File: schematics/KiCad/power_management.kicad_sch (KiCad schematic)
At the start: 19 parts, among them J3 USB_C, Q1 DMG6601LVT-7, U2 AP2112K-3.3, U4 CH340C, U5 MP2615AGQ-Z

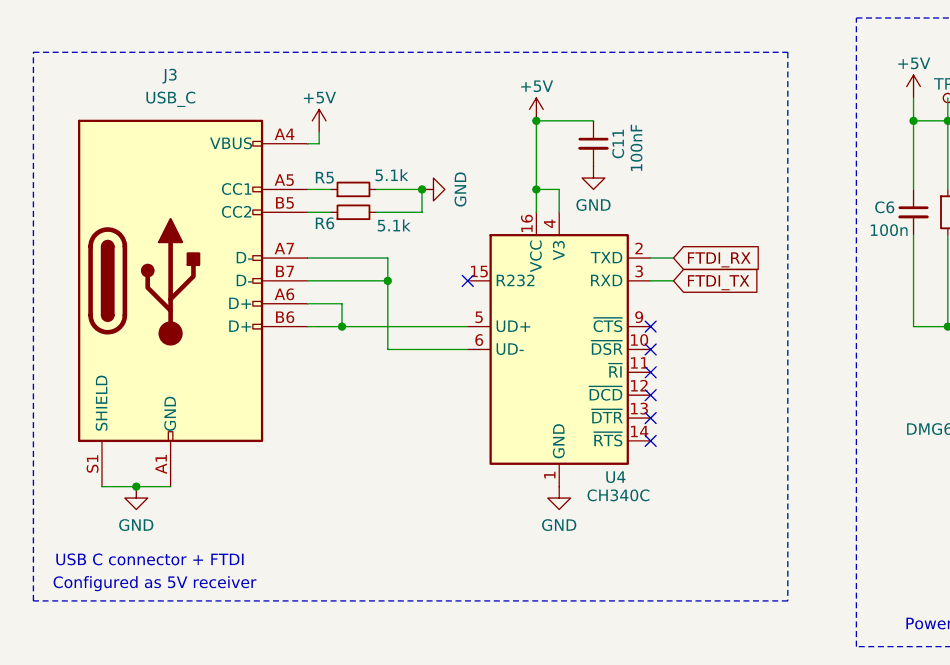
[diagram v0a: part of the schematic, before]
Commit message: move FTDI chip back to main page
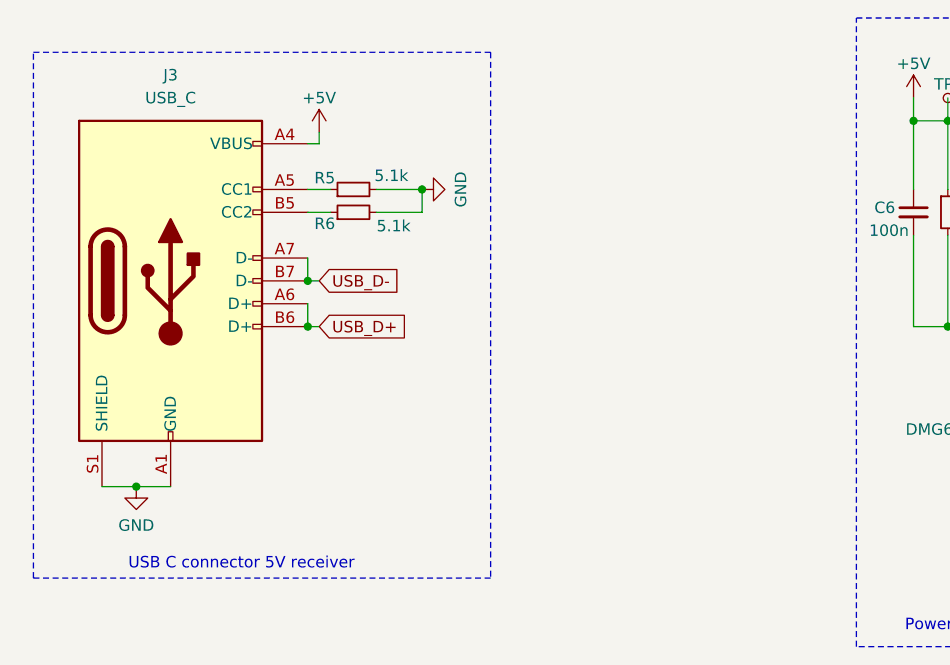
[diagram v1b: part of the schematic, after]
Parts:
- removed C11: 100nF, Capacitor_SMD:C_0201_0603Metric, symbol Device:C_Small
- removed U4: CH340C, Package_SO:SOIC-16_3.9x9.9mm_P1.27mm, symbol Interface_USB:CH340C
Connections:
- net USB_D+: now reaches J3.A6 (D+), J3.B6 (D+)
- net USB_D-: now reaches J3.A7 (D-), J3.B7 (D-)
- no-connect marks 7 -> 0
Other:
- note added: "USB C connector 5V receiver"
- note removed: "Configured as 5V receiver"
- note removed: "USB C connector + FTDI"

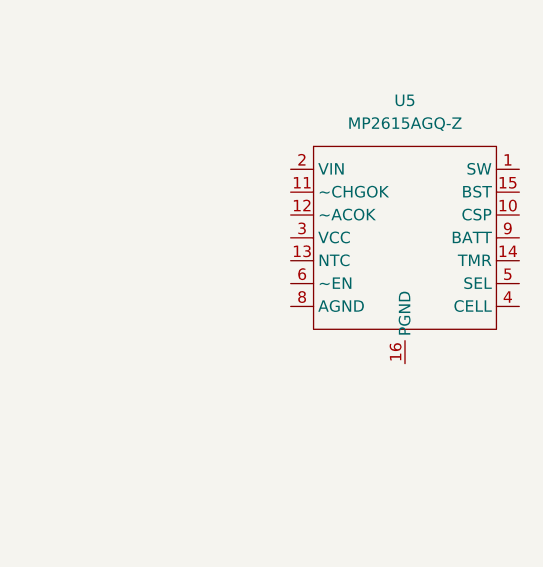
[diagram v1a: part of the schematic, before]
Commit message: reorganise symbols
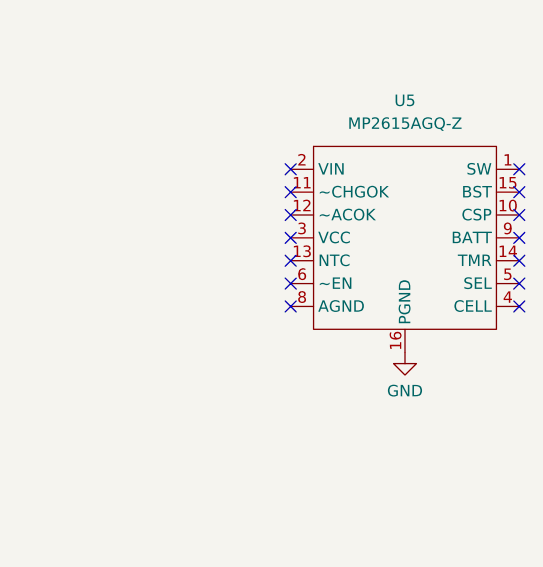
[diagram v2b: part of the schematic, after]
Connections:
- net GND: now also U5.16 (PGND)
- net at U5.7 (NC): no longer U5.16 (PGND)
- no-connect marks 0 -> 14
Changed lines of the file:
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@@
 		(color 0 0 0 0)
+	)
+	(no_connect
+		(at 252.73 91.44)
+	)
+	(no_connect
+		(at 227.33 99.06)
+	)
+	(no_connect
+		(at 227.33 91.44)
+	)
+	(no_connect
+		(at 227.33 88.9)
+	)
+	(no_connect
+		(at 252.73 86.36)
+	)
+	(no_connect
+		(at 227.33 96.52)
+	)
+	(no_connect
+		(at 252.73 96.52)
+	)
+	(no_connect
+		(at 252.73 88.9)
+	)
+	(no_connect
+		(at 252.73 93.98)
+	)
+	(no_connect
+		(at 227.33 86.36)
+	)
+	(no_connect
+		(at 252.73 99.06)
+	)
+	(no_connect
+		(at 227.33 93.98)
+	)
+	(no_connect
+		(at 227.33 101.6)
+	)
+	(no_connect
+		(at 252.73 101.6)
 	)
 	(wire
@@
 	)
 	(symbol
-		(lib_id "leany-symbols:DMG6601LVT-7")
-		(at 139.7 72.39 270)
-		(mirror x)
-		(unit 2)
-		(exclude_from_sim no)
-		(in_bom yes)
-		(on_board yes)
-		(dnp no)
-		(property "Reference" "Q1"
-			(at 139.7 66.04 90)
-			(effects
-				(font
-					(size 1.27 1.27)
-				)
-			)
-		)
-		(property "Value" "DMG6601LVT-7"
-			(at 139.7 68.58 90)
-			(effects
-				(font
-					(size 1.27 1.27)
-				)
-			)
-		)
-		(property "Footprint" "Package_TO_SOT_SMD:TSOT-23-6"
-			(at 137.795 69.85 0)
-			(effects
-				(font
-					(size 1.27 1.27)
-				)
-				(justify left)
-				(hide yes)
-			)
-		)
-		(property "Datasheet" "https://www.diodes.com/assets/Datasheets/DMG6601LVT.pdf"
-			(at 135.89 69.85 0)
-			(effects
-				(font
-					(size 1.27 1.27)
-				)
-				(justify left)
-				(hide yes)
-			)
-		)
-		(property "Description" "3.6A/-2.1A Id, 30V Vds, Complementary pair enhancement mode P-Channel and N-Channel MOSFET, TSOT-23-6"
-			(at 139.7 72.39 0)
-			(effects
-				(font
-					(size 1.27 1.27)
-				)
-				(hide yes)
-			)
-		)
-		(pin "1"
-		)
-		(pin "2"
-		)
-		(pin "3"
-		)
-		(pin "4"
-		)
-		(pin "5"
-		)
-		(pin "6"
-		)
-		(instances
-			(project "leany"
-				(path "/e47b2519-93ca-4a48-9414-ecc253dd35f5/702fc064-eab2-4b82-8f62-a654ccd28f72"
-					(reference "Q1")
-					(unit 2)
-				)
-			)
-		)
-	)
-	(symbol
-		(lib_id "Device:R_Small")
-		(at 149.86 113.03 180)
-		(unit 1)
-		(exclude_from_sim no)
-		(in_bom yes)
-		(on_board yes)
-		(dnp no)
-		(property "Reference" "R4"
-			(at 145.796 111.76 90)
-			(effects
-				(font
-					(size 1.27 1.27)
-				)
-				(justify left)
-			)
-		)
-		(property "Value" "1M"
-			(at 147.828 111.506 90)
-			(effects
-				(font
-					(size 1.27 1.27)
-				)
-				(justify left)
-			)
-		)
-		(property "Footprint" "Resistor_SMD:R_0603_1608Metric"
-			(at 149.86 113.03 0)
-			(effects
-				(font
-					(size 1.27 1.27)
-				)
-				(hide yes)
-			)
-		)
-		(property "Datasheet" "~"
-			(at 149.86 113.03 0)
-			(effects
-				(font
-					(size 1.27 1.27)
-				)
-				(hide yes)
-			)
-		)
-		(property "Description" "Resistor, small symbol"
-			(at 149.86 113.03 0)
-			(effects
-				(font
-					(size 1.27 1.27)
-				)
-				(hide yes)
-			)
-		)
-		(pin "1"
-		)
-		(pin "2"
-		)
-		(instances
-			(project "leany"
-				(path "/e47b2519-93ca-4a48-9414-ecc253dd35f5/702fc064-eab2-4b82-8f62-a654ccd28f72"
-					(reference "R4")
-					(unit 1)
-				)
-			)
-		)
-	)
-	(symbol
 		(lib_id "leany-symbols:MP2615AGQ-Z")
 		(at 240.03 93.98 0)
@@
 			)
 		)
+		(pin "14"
+		)
 		(pin "4"
 		)
+		(pin "5"
+		)
+		(pin "11"
+		)
+		(pin "8"
+		)
+		(pin "13"
+		)
+		(pin "9"
+		)
 		(pin "7"
 		)
-		(pin "9"
+		(pin "10"
+		)
+		(pin "12"
+		)
+		(pin "1"
+		)
+		(pin "2"
+		)
+		(pin "6"
+		)
+		(pin "3"
 		)
 		(pin "15"
 		)
-		(pin "10"
+		(pin "16"
+		)
+		(instances
+			(project ""
+				(path "/e47b2519-93ca-4a48-9414-ecc253dd35f5/702fc064-eab2-4b82-8f62-a654ccd28f72"
+					(reference "U5")
+					(unit 1)
+				)
+			)
+		)
+	)
+	(symbol
+		(lib_id "leany-symbols:DMG6601LVT-7")
+		(at 139.7 72.39 270)
+		(mirror x)
+		(unit 2)
+		(exclude_from_sim no)
+		(in_bom yes)
+		(on_board yes)
+		(dnp no)
+		(property "Reference" "Q1"
+			(at 139.7 66.04 90)
+			(effects
+				(font
+					(size 1.27 1.27)
+				)
+			)
+		)
+		(property "Value" "DMG6601LVT-7"
+			(at 139.7 68.58 90)
+			(effects
+				(font
+					(size 1.27 1.27)
+				)
+			)
+		)
+		(property "Footprint" "Package_TO_SOT_SMD:TSOT-23-6"
+			(at 137.795 69.85 0)
+			(effects
+				(font
+					(size 1.27 1.27)
+				)
+				(justify left)
+				(hide yes)
+			)
+		)
+		(property "Datasheet" "https://www.diodes.com/assets/Datasheets/DMG6601LVT.pdf"
+			(at 135.89 69.85 0)
+			(effects
+				(font
+					(size 1.27 1.27)
+				)
+				(justify left)
+				(hide yes)
+			)
+		)
+		(property "Description" "3.6A/-2.1A Id, 30V Vds, Complementary pair enhancement mode P-Channel and N-Channel MOSFET, TSOT-23-6"
+			(at 139.7 72.39 0)
+			(effects
+				(font
+					(size 1.27 1.27)
+				)
+				(hide yes)
+			)
+		)
+		(pin "1"
 		)
 		(pin "2"
 		)
-		(pin "1"
-		)
-		(pin "12"
-		)
-		(pin "14"
-		)
-		(pin "8"
-		)
-		(pin "13"
-		)
-		(pin "16"
+		(pin "3"
+		)
+		(pin "4"
+		)
+		(pin "5"
 		)
 		(pin "6"
-		)
-		(pin "11"
-		)
-		(pin "3"
-		)
-		(pin "5"
 		)
 		(instances
 			(project "leany"
 				(path "/e47b2519-93ca-4a48-9414-ecc253dd35f5/702fc064-eab2-4b82-8f62-a654ccd28f72"
-					(reference "U5")
+					(reference "Q1")
+					(unit 2)
+				)
+			)
+		)
+	)
+	(symbol
+		(lib_id "Device:R_Small")
+		(at 149.86 113.03 180)
+		(unit 1)
+		(exclude_from_sim no)
+		(in_bom yes)
+		(on_board yes)
+		(dnp no)
+		(property "Reference" "R4"
+			(at 145.796 111.76 90)
+			(effects
+				(font
+					(size 1.27 1.27)
+				)
+				(justify left)
+			)
+		)
+		(property "Value" "1M"
+			(at 147.828 111.506 90)
+			(effects
+				(font
+					(size 1.27 1.27)
+				)
+				(justify left)
+			)
+		)
+		(property "Footprint" "Resistor_SMD:R_0603_1608Metric"
+			(at 149.86 113.03 0)
+			(effects
+				(font
+					(size 1.27 1.27)
+				)
+				(hide yes)
+			)
+		)
+		(property "Datasheet" "~"
+			(at 149.86 113.03 0)
+			(effects
+				(font
+					(size 1.27 1.27)
+				)
+				(hide yes)
+			)
+		)
+		(property "Description" "Resistor, small symbol"
+			(at 149.86 113.03 0)
+			(effects
+				(font
+					(size 1.27 1.27)
+				)
+				(hide yes)
+			)
+		)
+		(pin "1"
+		)
+		(pin "2"
+		)
+		(instances
+			(project "leany"
+				(path "/e47b2519-93ca-4a48-9414-ecc253dd35f5/702fc064-eab2-4b82-8f62-a654ccd28f72"
+					(reference "R4")
 					(unit 1)
 				)
@@
 					(unit 1)
 				)
+			)
+		)
+	)
+	(symbol
+		(lib_id "power:GND")
+		(at 240.03 106.68 0)
+		(unit 1)
+		(exclude_from_sim no)
+		(in_bom yes)
+		(on_board yes)
+		(dnp no)
+		(property "Reference" "#PWR028"
+			(at 240.03 113.03 0)
+			(effects
+				(font
+					(size 1.27 1.27)
+				)
+				(hide yes)
+			)
+		)
+		(property "Value" "GND"
+			(at 240.03 110.998 0)
+			(effects
+				(font
+					(size 1.27 1.27)
+				)
+			)
+		)
+		(property "Footprint" ""
+			(at 240.03 106.68 0)
+			(effects
+				(font
+					(size 1.27 1.27)
+				)
+				(hide yes)
+			)
+		)
+		(property "Datasheet" ""
+			(at 240.03 106.68 0)
+			(effects
+				(font
+					(size 1.27 1.27)
+				)
+				(hide yes)
+			)
+		)
+		(property "Description" "Power symbol creates a global label with name \"GND\" , ground"
+			(at 240.03 106.68 0)
+			(effects
+				(font
+					(size 1.27 1.27)
+				)
+				(hide yes)
+			)
+		)
+		(pin "1"
+		)
+		(instances
+			(project "leany"
+				(path "/e47b2519-93ca-4a48-9414-ecc253dd35f5/702fc064-eab2-4b82-8f62-a654ccd28f72"
+					(reference "#PWR028")
+					(unit 1)
+				)

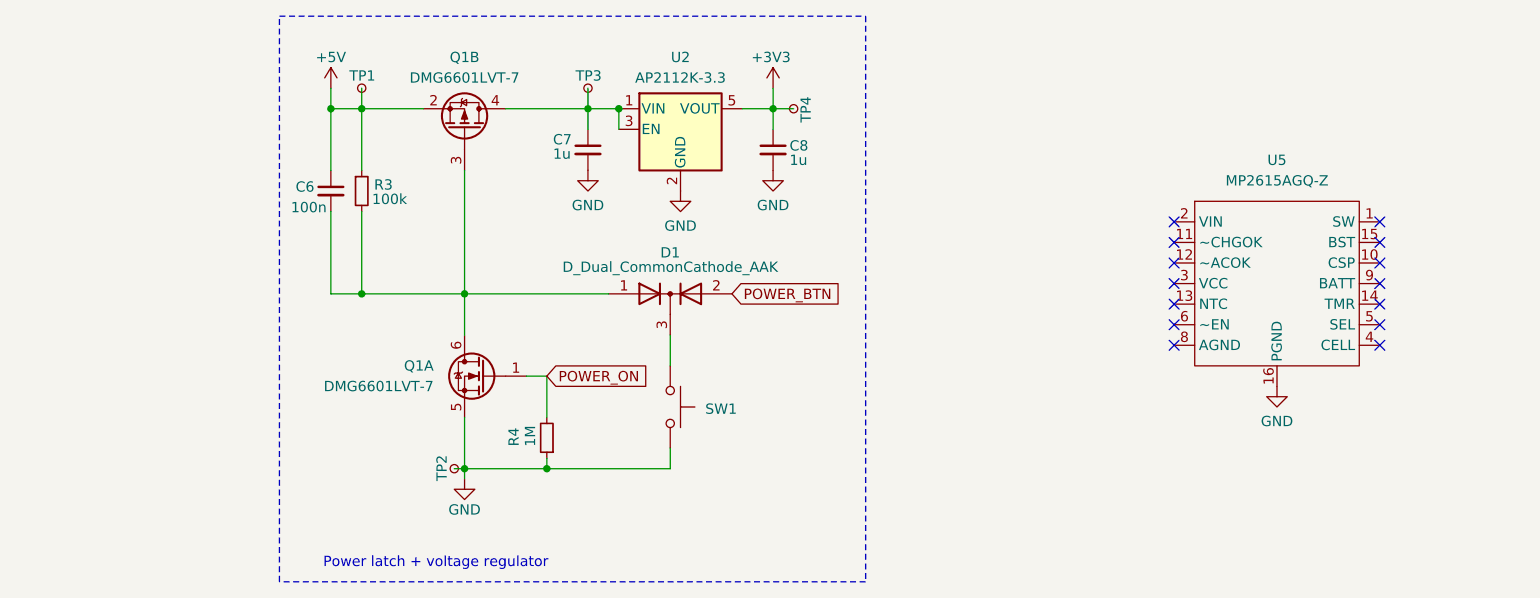
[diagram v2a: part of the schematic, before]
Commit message: wire up the charge controller
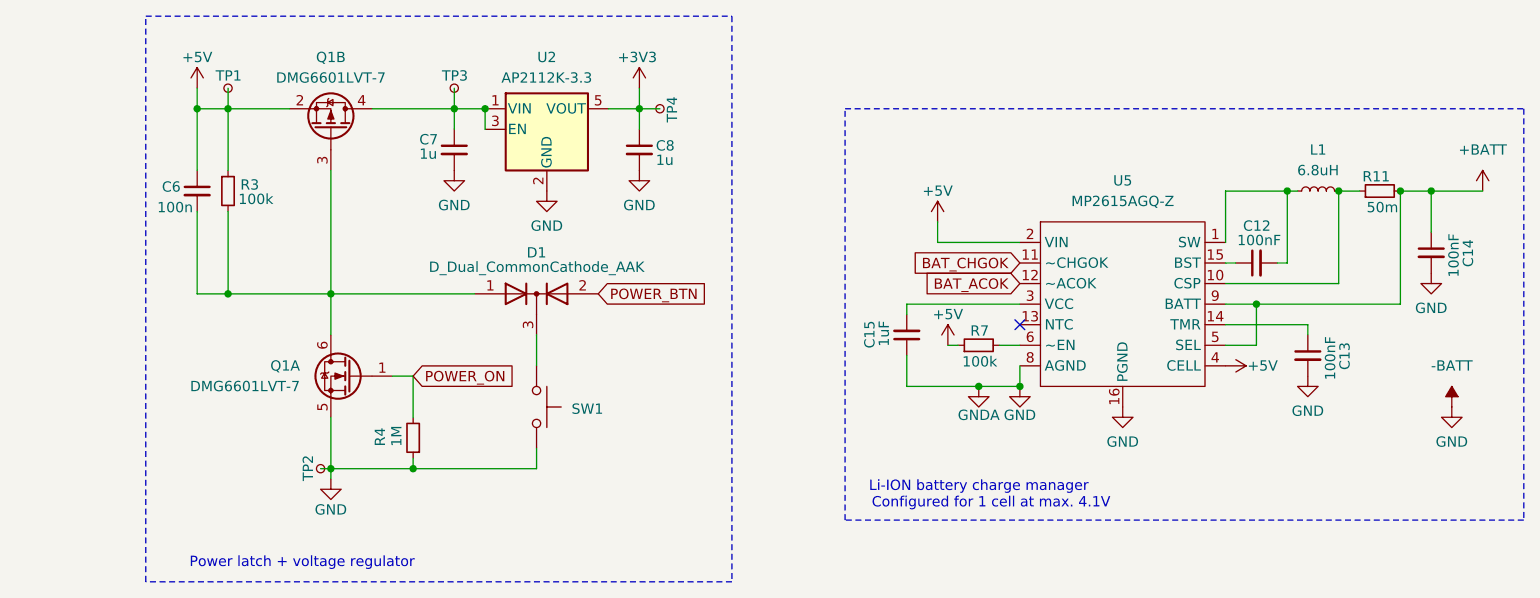
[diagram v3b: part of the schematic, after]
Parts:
- added C12, C13, C14: 100nF, Capacitor_SMD:C_0201_0603Metric, symbol Device:C_Small
- added C15: 1uF, Capacitor_SMD:C_0201_0603Metric, symbol Device:C_Small
- added L1: 6.8uH, symbol Device:L_Small
- added R11: 50m, Resistor_SMD:R_0603_1608Metric, symbol Device:R_Small
- added R7: 100k, Resistor_SMD:R_0603_1608Metric, symbol Device:R_Small
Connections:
- net GND is gone; now on net -BATT: C7.2, C8.2, J3.A1 (GND), J3.A12 (GND), J3.B1 (GND), J3.B12 (GND), J3.S1 (SHIELD), Q1.5 (S), R4.1, R5.2, R6.2, SW1.2, TP2.1, U2.2 (GND), U5.16 (PGND)
- net +5V: now also U5.2 (VIN), U5.4 (CELL), R7.1
- net at U5.1 (SW): now also C12.2, L1.1
- net at U5.10 (CSP): now also L1.2, R11.1
- net BAT_CHGOK: now reaches U5.11 (~CHGOK)
- net BAT_ACOK: now reaches U5.12 (~ACOK)
- net at U5.14 (TMR): now also C13.1
- net at U5.15 (BST): now also C12.1
- net at U5.3 (VCC): now also C15.2
- net +BATT: now reaches U5.5 (SEL)
- net +BATT: now also U5.9 (BATT), C14.1, R11.2
- net at U5.6 (~EN): now also R7.2
- net -BATT: now reaches U5.8 (AGND)
- net -BATT: now also C13.2, C14.2, C15.1
- no-connect marks 14 -> 1
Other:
- note added: "Configured for 1 cell at max. 4.1V"
- note added: "Li-ION battery charge manager"
- moved on the sheet: C6, C7, C8, D1, Q1A, Q1B, R3, R4, SW1, TP1, TP2, TP3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

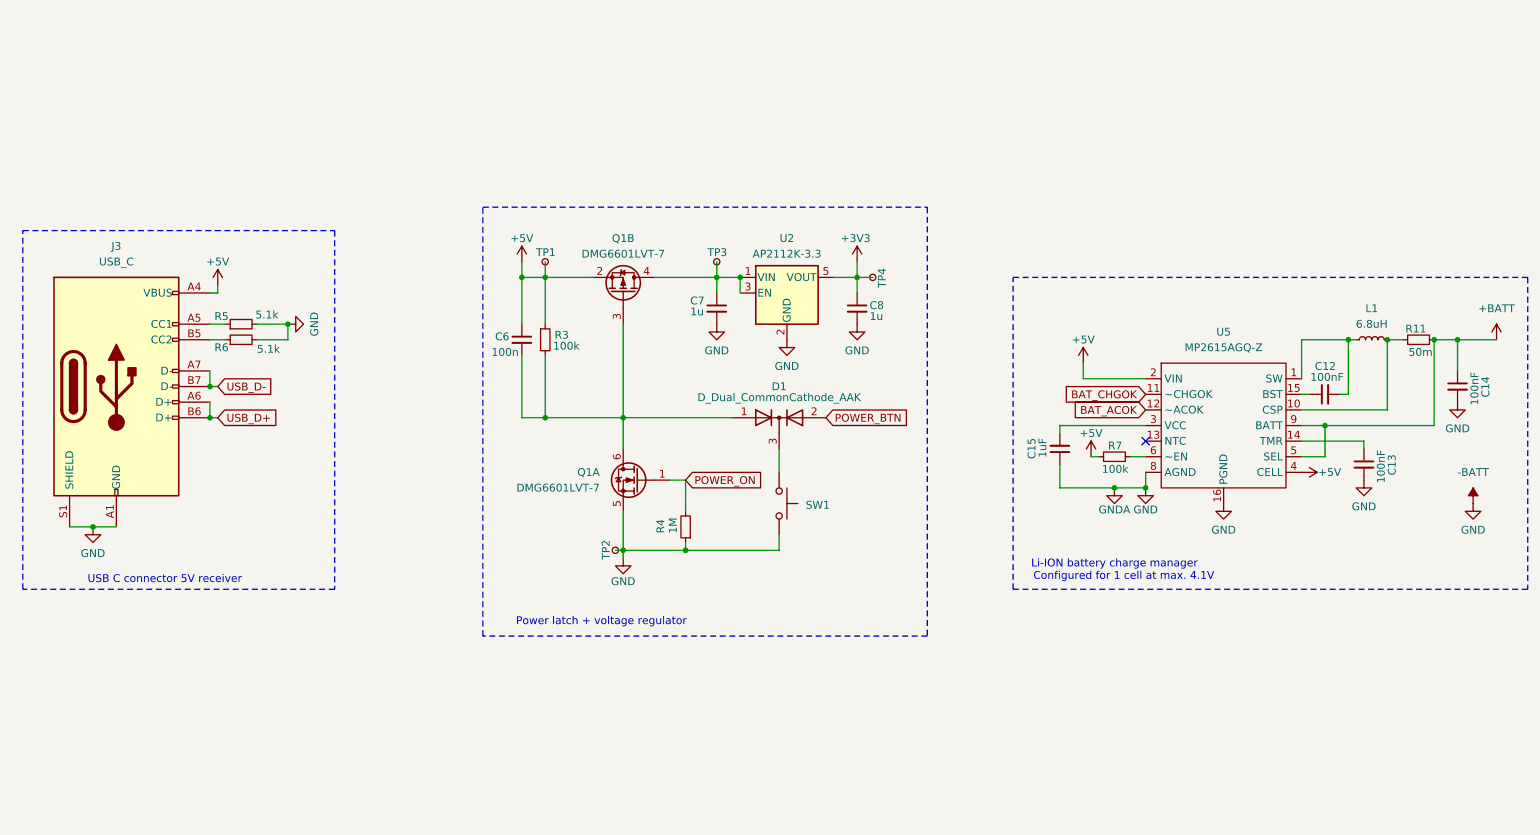
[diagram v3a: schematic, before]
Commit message: indicate a direct wiring of USB output
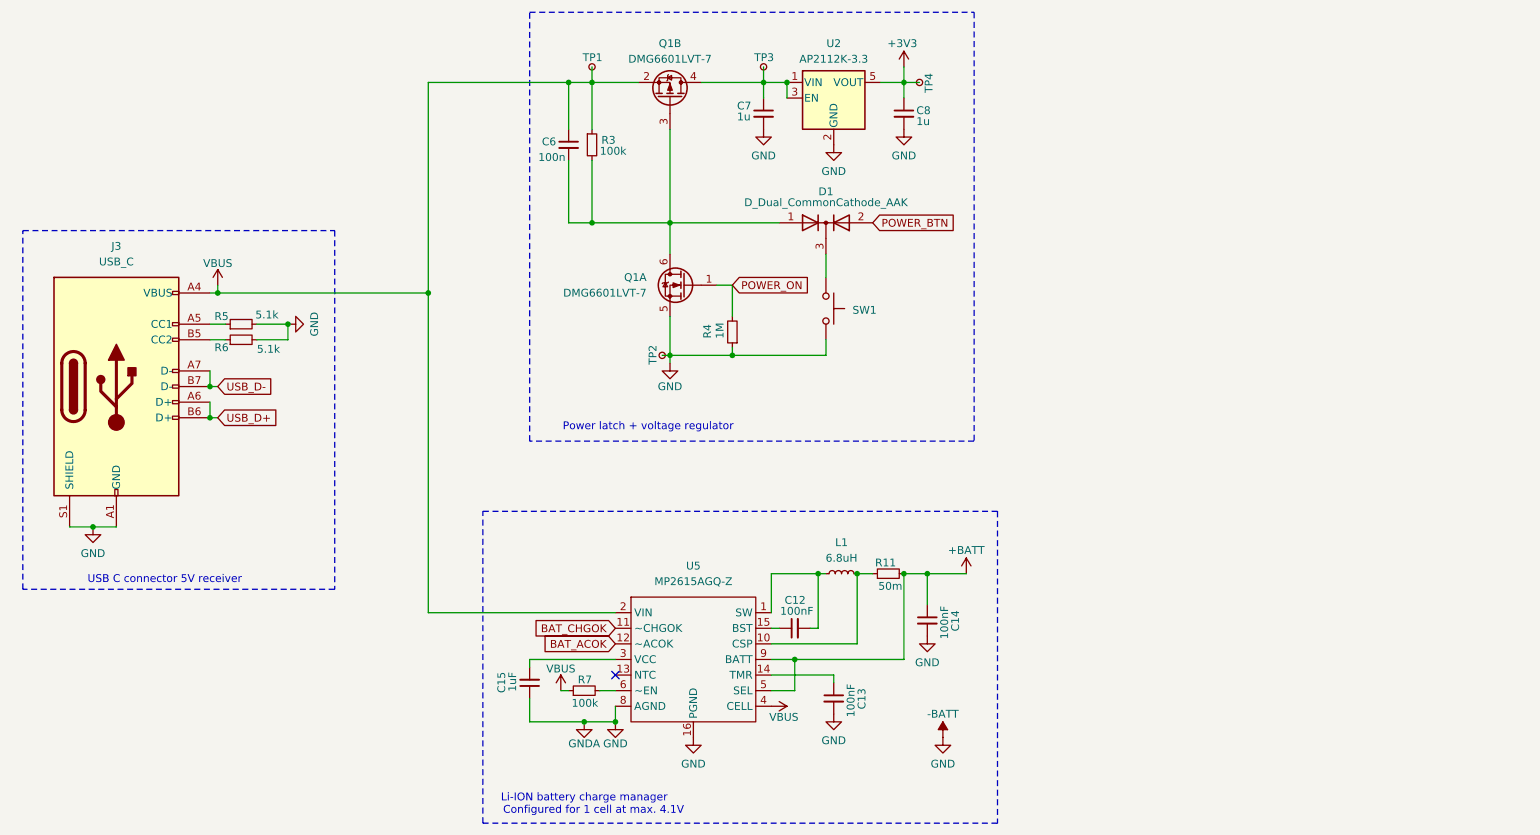
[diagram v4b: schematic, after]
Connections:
- net +5V renamed VBUS
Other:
- moved on the sheet: C12, C13, C14, C15, C6, C7, C8, D1, L1, Q1A, Q1B, R11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

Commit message: clear annotations
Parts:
- renumbered C14 to C?, C15 to C?, C6 to C?, C7 to C?, C13 to C?, C8 to C?, C12 to C?, D1 to D?, J3 to J?, L1 to L?, Q1 to Q?, R4 to R?, R5 to R?, R3 to R?, R7 to R?, R11 to R?, R6 to R?, SW1 to SW?, TP1 to TP?, TP3 to TP?, TP4 to TP?, TP2 to TP?, U5 to U?, U2 to U?

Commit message: re-annotate components
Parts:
- gave numbers to parts that had none: 24
